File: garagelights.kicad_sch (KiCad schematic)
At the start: 32 parts, among them J1 Conn_01x04, Q1 Q_NMOS_GDS, Q2 Q_NMOS_GDS, Q3 Q_NMOS_GDS, U1 NE555P, U2 NE555P, U3 4013, U4 4013

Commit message: mostly finished layout
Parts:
- removed D2: GREEN, symbol Device:LED
- removed D3: YELLOW, symbol Device:LED
- removed D6: RED, symbol Device:LED
- removed R3, R7, R9: 220, symbol Device:R_US
- added C6, C7: 0.1, Capacitor_THT:C_Disc_D5.0mm_W2.5mm_P2.50mm, symbol Device:C
- added J2: Conn_01x06, Connector_PinSocket_2.54mm:PinSocket_1x06_P2.54mm_Vertical, symbol Connector_Generic:Conn_01x06
- added RV1, RV2: 10k, Potentiometer_THT:Potentiometer_Bourns_3386P_Vertical, symbol Device:R_Potentiometer_US
- added U4: LM7805_TO220, Package_TO_SOT_THT:TO-220-3_Vertical, symbol Regulator_Linear:LM7805_TO220
- C1, C2, C3, C4: footprint (none) -> Capacitor_THT:C_Disc_D5.0mm_W2.5mm_P2.50mm
- C10: renamed from C8; footprint (none) -> Capacitor_THT:C_Disc_D5.0mm_W2.5mm_P2.50mm
- C5: value 0.1 uF -> 0.1; footprint (none) -> Capacitor_THT:C_Disc_D5.0mm_W2.5mm_P2.50mm
- C8: renamed from C6; value 0.1 uF -> 0.1; footprint (none) -> Capacitor_THT:C_Disc_D5.0mm_W2.5mm_P2.50mm
- C9: renamed from C7; footprint (none) -> Capacitor_THT:C_Disc_D5.0mm_W2.5mm_P2.50mm
- D1: value D -> 1N914; footprint (none) -> Diode_THT:D_DO-35_SOD27_P7.62mm_Horizontal
- J1: footprint (none) -> Connector_PinSocket_2.54mm:PinSocket_1x04_P2.54mm_Vertical
- Q1: value Q_NMOS_GDS -> ZVN4206AV; footprint (none) -> Package_TO_SOT_THT:TO-92S; symbol Transistor_FET:Q_NMOS_GDS -> Transistor_FET:Q_NMOS_DGS
- Q2, Q3: value Q_NMOS_GDS -> ZVN4206AV; footprint (none) -> Package_TO_SOT_THT:TO-92S
- R1, R2: footprint (none) -> Resistor_THT:R_Axial_DIN0204_L3.6mm_D1.6mm_P7.62mm_Horizontal
- R3: renamed from R4; footprint (none) -> Resistor_THT:R_Axial_DIN0204_L3.6mm_D1.6mm_P7.62mm_Horizontal
- R4: renamed from R5; footprint (none) -> Resistor_THT:R_Axial_DIN0204_L3.6mm_D1.6mm_P7.62mm_Horizontal
- R5: renamed from R6; footprint (none) -> Resistor_THT:R_Axial_DIN0204_L3.6mm_D1.6mm_P7.62mm_Horizontal
- R6: renamed from R8; footprint (none) -> Resistor_THT:R_Axial_DIN0204_L3.6mm_D1.6mm_P7.62mm_Horizontal
- R7: renamed from R10; footprint (none) -> Resistor_THT:R_Axial_DIN0204_L3.6mm_D1.6mm_P7.62mm_Horizontal
- U1, U2: footprint Package_DIP:DIP-8_W7.62mm -> Package_DIP:DIP-8_W7.62mm_Socket
- U3: footprint (none) -> Package_DIP:DIP-14_W7.62mm_Socket
- U5: renamed from U4; footprint (none) -> Package_DIP:DIP-14_W7.62mm_Socket
- renumbered D4 to D2, D5 to D3
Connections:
- net VDD is gone; now on net +5V: U3.5 (D), U5.5 (D)
- net +5V: now also C6.1, U4.3 (VO)
- net GND: now also C6.2, C7.2, J2.6 (Pin_6), U4.2 (GND)
- net at C8.1, U5.4 (R): now also RV2.3; no longer R7.2
- net at C5.1, U3.4 (R): now also RV1.3; no longer R5.2
- net at Q2.2 (D): now also J2.4 (Pin_4)
- net at Q3.2 (D): now also J2.5 (Pin_5)
- net at Q1.1 (D): now also J2.3 (Pin_3); no longer U3.13 (Q)
- net at Q1.2 (G): now also U3.13 (Q)
- new net: R7.2, RV2.1, RV2.2
- new net: R5.2, RV1.1, RV1.2
- new net +12V: C7.1, J2.1 (Pin_1), U4.1 (VI)
- no-connect marks 1 -> 2
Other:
- note added: "Adafruit #2993: Tower Light - Red Yellow Green Alert Light with Buzzer - 12VDC"
- note added: "C320C104J3G5TA"
- note added: "GREEN"
- note added: "HC-SR04 ultrasonic range finder"
- note added: "RED"
- note added: "TAP104K035SCS"
- note added: "YELLOW"
- note added: "buzzer not connected"
- moved on the sheet: C5, C8, D2, D3, Q1, Q2, Q3, R6, R7, U5A, U5B

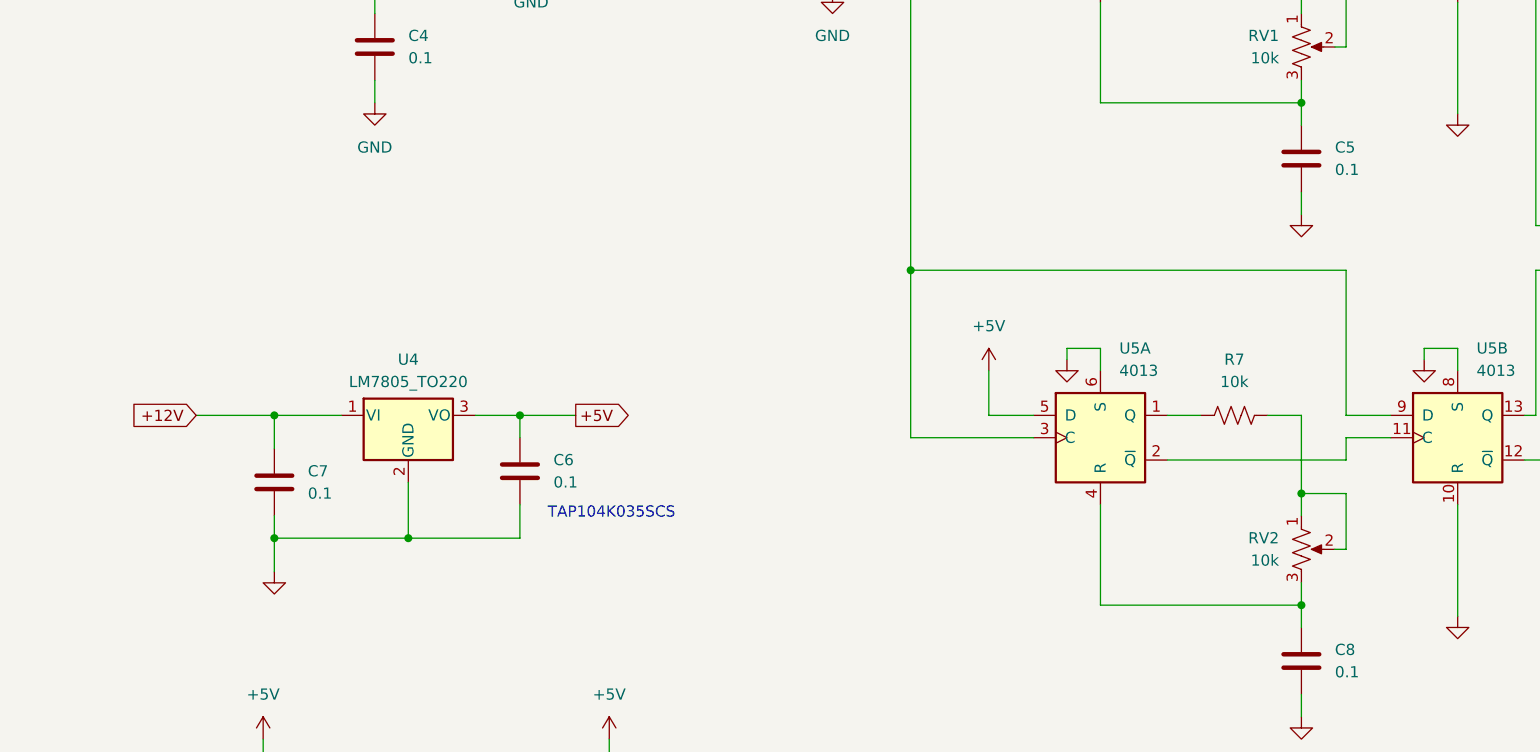
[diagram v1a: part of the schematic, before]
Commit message: Added screw terminals and mounting holes
Also working towards reducing the number of layers to two.
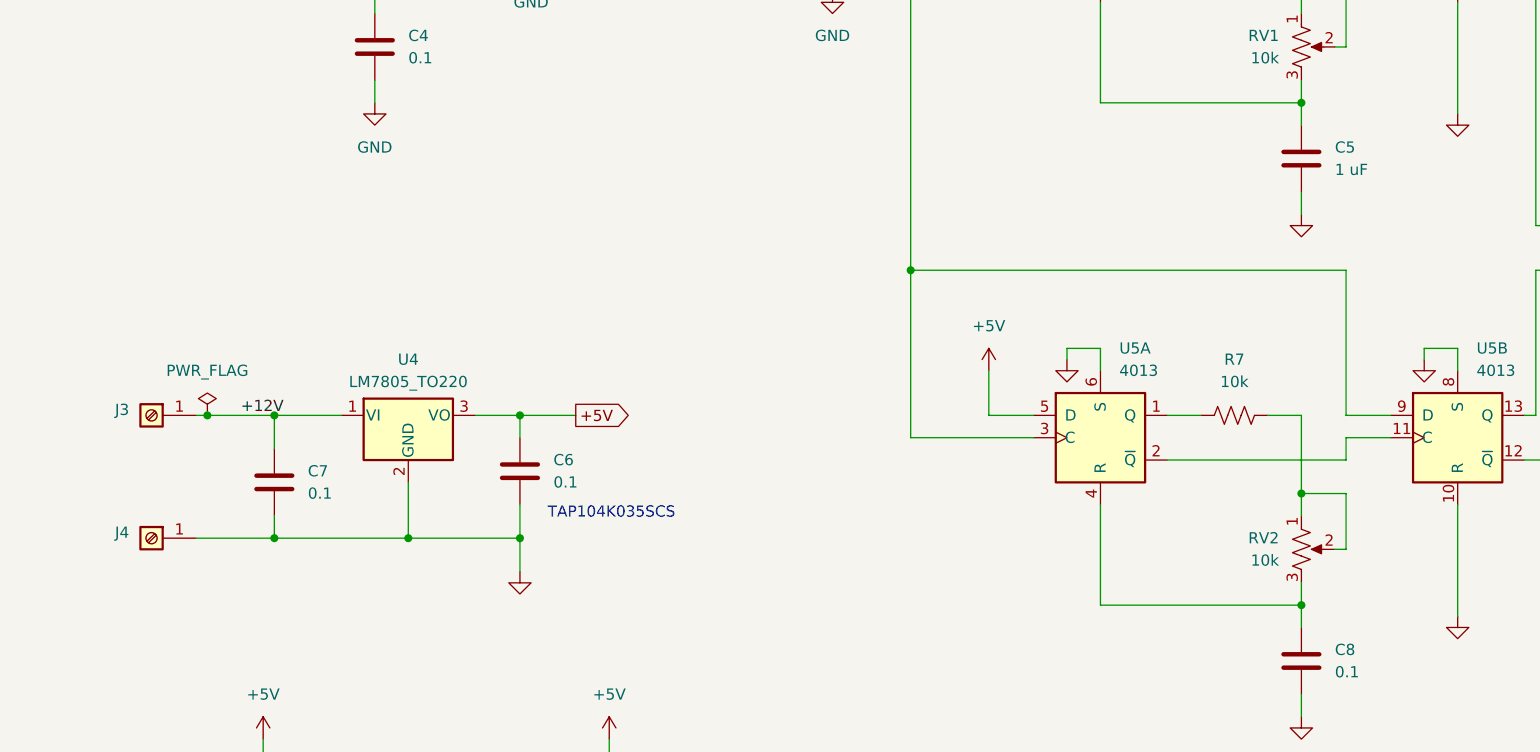
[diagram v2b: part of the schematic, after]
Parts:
- added J3, J4: Screw_Terminal_01x01, Library:KEYSTONE_8191, symbol Connector:Screw_Terminal_01x01
- C5: value 0.1 -> 1 uF
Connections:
- net +12V: now also J3.1 (Pin_1)
- net GND: now also J4.1 (Pin_1)

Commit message: Kinda sorta Rev_A
Finished the layout and brought it down to two layers, one of which
is a ground plane. Imported missing 3D models.
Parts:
- added C11, C12: 0.1, Capacitor_THT:C_Disc_D5.0mm_W2.5mm_P2.50mm, symbol Device:C
- Q2, Q3: symbol Transistor_FET:Q_NMOS_GDS -> Transistor_FET_Other:Q_NMOS_Depletion_DGS
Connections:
- net +5V: now also C11.1, C12.1
- net GND: now also C11.2, C12.2
- net at D2.2 (A), D3.2 (A), R6.2: now also Q2.2 (G); no longer Q2.1 (G)
- net at Q3.1 (D): now also J2.5 (Pin_5); no longer U5.12 (~{Q})
- net at Q3.2 (G): now also U5.12 (~{Q}); no longer J2.5 (Pin_5)
- net at J2.4 (Pin_4): now also Q2.1 (D); no longer Q2.2 (D)

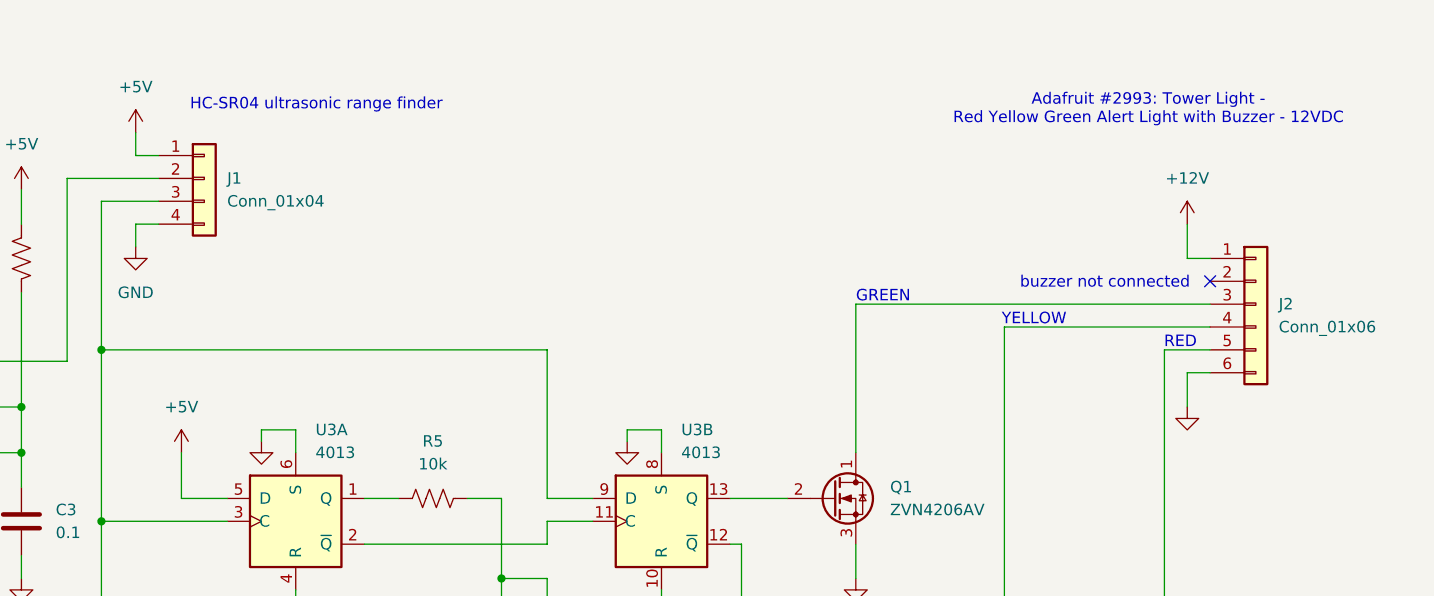
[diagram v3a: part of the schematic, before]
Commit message: Spec Samtec connectors for the socket headers.
Also more fussing with position and text.
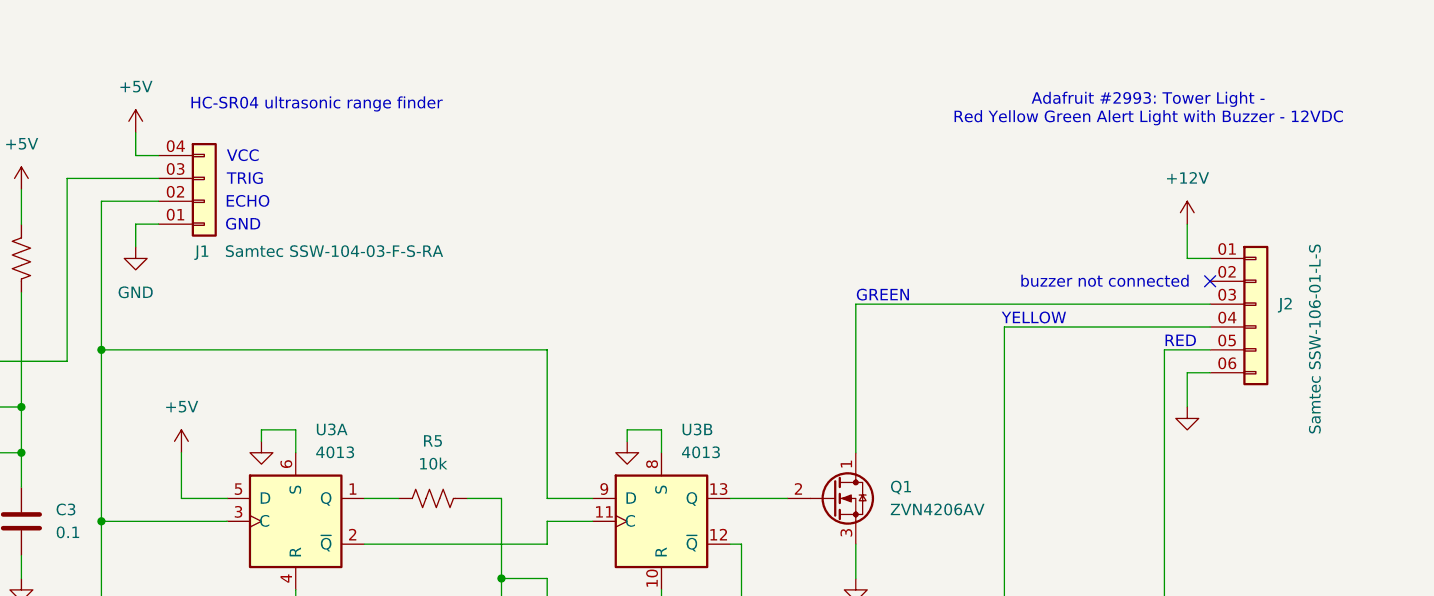
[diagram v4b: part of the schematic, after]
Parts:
- J1: value Conn_01x04 -> Samtec SSW-104-03-F-S-RA; footprint Connector_PinSocket_2.54mm:PinSocket_1x04_P2.54mm_Vertical -> Library:SAMTEC_SSW-104-03-F-S-RA
- J2: value Conn_01x06 -> Samtec SSW-106-01-L-S; footprint Connector_PinSocket_2.54mm:PinSocket_1x06_P2.54mm_Vertical -> Library:SAMTEC_SSW-106-01-X-S
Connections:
- net +12V: now also J2.01 (Pin_1); no longer J2.1 (Pin_1)
- net +5V: now also J1.04 (Pin_1); no longer J1.1 (Pin_1)
- net GND: now also J1.01 (Pin_4), J2.06 (Pin_6); no longer J1.4 (Pin_4), J2.6 (Pin_6)
- net at Q3.1 (D): now also J2.05 (Pin_5); no longer J2.5 (Pin_5)
- net at U3.3 (C), U3.9 (D), U5.3 (C)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: now also J1.02 (Pin_3); no longer J1.3 (Pin_3)
- net at U2.3 (Q): now also J1.03 (Pin_2); no longer J1.2 (Pin_2)
- net at Q2.1 (D): now also J2.04 (Pin_4); no longer J2.4 (Pin_4)
- net at Q1.1 (D): now also J2.03 (Pin_3); no longer J2.3 (Pin_3)
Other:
- note added: "ECHO"
- note added: "GND"
- note added: "TRIG"
- note added: "VCC"
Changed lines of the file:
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@@
 		)
 	)
+	(text "VCC"
+		(exclude_from_sim no)
+		(at 140.208 30.734 0)
+		(effects
+			(font
+				(size 1.27 1.27)
+			)
+		)
+	)
+	(text "ECHO"
+		(exclude_from_sim no)
+		(at 140.716 35.814 0)
+		(effects
+			(font
+				(size 1.27 1.27)
+			)
+		)
+	)
 	(text "Adafruit #2993: Tower Light - \nRed Yellow Green Alert Light with Buzzer - 12VDC"
 		(exclude_from_sim no)
@@
 		)
 	)
+	(text "GND"
+		(exclude_from_sim no)
+		(at 140.208 38.354 0)
+		(effects
+			(font
+				(size 1.27 1.27)
+			)
+		)
+	)
 	(text "buzzer not connected"
 		(exclude_from_sim no)
@@
 		)
 	)
+	(text "TRIG"
+		(exclude_from_sim no)
+		(at 140.462 33.274 0)
+		(effects
+			(font
+				(size 1.27 1.27)
+			)
+		)
+	)
 	(text "YELLOW"
 		(exclude_from_sim no)
@@
 		(on_board yes)
 		(dnp no)
-		(fields_autoplaced yes)
 		(property "Reference" "J1"
-			(at 138.43 33.0199 0)
+			(at 134.874 41.148 0)
 			(effects
 				(font
@@
 			)
 		)
-		(property "Value" "Conn_01x04"
-			(at 138.43 35.5599 0)
+		(property "Value" "Samtec SSW-104-03-F-S-RA"
+			(at 138.176 41.148 0)
 			(effects
 				(font
@@
 			)
 		)
-		(property "Footprint" "Connector_PinSocket_2.54mm:PinSocket_1x04_P2.54mm_Vertical"
+		(property "Footprint" "Library:SAMTEC_SSW-104-03-F-S-RA"
 			(at 135.89 33.02 0)
 			(effects
@@
 			)
 		)
-		(pin "2"
+		(pin "04"
 		)
-		(pin "3"
+		(pin "02"
 		)
-		(pin "4"
+		(pin "03"
 		)
-		(pin "1"
+		(pin "01"
 		)
 		(instances
@@
 		(on_board yes)
 		(dnp no)
-		(fields_autoplaced yes)
 		(property "Reference" "J2"
 			(at 255.27 46.9899 0)
@@
 			)
 		)
-		(property "Value" "Conn_01x06"
-			(at 255.27 49.5299 0)
+		(property "Value" "Samtec SSW-106-01-L-S"
+			(at 259.334 61.468 90)
 			(effects
 				(font
@@
 			)
 		)
-		(property "Footprint" "Connector_PinSocket_2.54mm:PinSocket_1x06_P2.54mm_Vertical"
+		(property "Footprint" "Library:SAMTEC_SSW-106-01-X-S"
 			(at 252.73 46.99 0)
 			(effects
@@
 			)
 		)
-		(pin "1"
+		(pin "05"
 		)
-		(pin "2"
+		(pin "02"
 		)
-		(pin "3"
+		(pin "06"
 		)
-		(pin "5"
+		(pin "04"
 		)
-		(pin "6"
+		(pin "03"
 		)
-		(pin "4"
+		(pin "01"
 		)
 		(instances
